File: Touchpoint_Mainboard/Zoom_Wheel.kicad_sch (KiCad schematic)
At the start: 7 parts

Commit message: Finished assigning footprints and 3d models for both boards
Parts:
- S1: footprint PEC12R-4220F-S0024:XDCR_PEC12R-4220F-S0024 -> Touchpoint:XDCR_PEC12R-4220F-S0024
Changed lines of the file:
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@@
 			)
 		)
-		(property "Footprint" "PEC12R-4220F-S0024:XDCR_PEC12R-4220F-S0024"
+		(property "Footprint" "Touchpoint:XDCR_PEC12R-4220F-S0024"
 			(at 68.58 38.1 0)
 			(effects

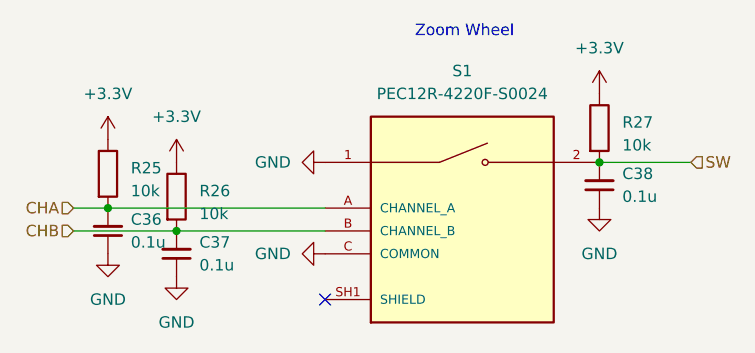
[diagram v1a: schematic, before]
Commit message: Added 3.3V to interface
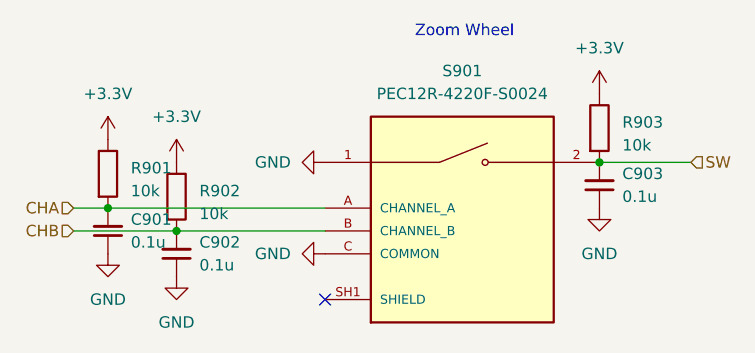
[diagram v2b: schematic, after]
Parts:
- renumbered C36 to C901, C37 to C902, C38 to C903, R25 to R901, R26 to R902, R27 to R903, S1 to S901
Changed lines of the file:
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@@
 		(dnp no)
 		(fields_autoplaced yes)
-		(property "Reference" "#PWR064"
+		(property "Reference" "#PWR0907"
 			(at 83.82 29.21 0)
 			(effects
@@
 			(project "Touchpoint_Mainboard"
 				(path "/f37b5f88-420a-4646-85df-8f9851d23e3c/eee90675-6c72-4499-ad3c-d412c9e5ddd7"
-					(reference "#PWR064")
+					(reference "#PWR0907")
 					(unit 1)
 				)
@@
 		(dnp no)
 		(fields_autoplaced yes)
-		(property "Reference" "#PWR069"
+		(property "Reference" "#PWR0906"
 			(at 46.99 43.18 0)
 			(effects
@@
 			(project "Touchpoint_Mainboard"
 				(path "/f37b5f88-420a-4646-85df-8f9851d23e3c/eee90675-6c72-4499-ad3c-d412c9e5ddd7"
-					(reference "#PWR069")
+					(reference "#PWR0906")
 					(unit 1)
 				)
@@
 		(dnp no)
 		(fields_autoplaced yes)
-		(property "Reference" "#PWR063"
+		(property "Reference" "#PWR0905"
 			(at 46.99 33.02 0)
 			(effects
@@
 			(project "Touchpoint_Mainboard"
 				(path "/f37b5f88-420a-4646-85df-8f9851d23e3c/eee90675-6c72-4499-ad3c-d412c9e5ddd7"
-					(reference "#PWR063")
+					(reference "#PWR0905")
 					(unit 1)
 				)
@@
 		(dnp no)
 		(fields_autoplaced yes)
-		(property "Reference" "#PWR072"
+		(property "Reference" "#PWR0902"
 			(at 29.21 49.53 0)
 			(effects
@@
 			(project "Touchpoint_Mainboard"
 				(path "/f37b5f88-420a-4646-85df-8f9851d23e3c/eee90675-6c72-4499-ad3c-d412c9e5ddd7"
-					(reference "#PWR072")
+					(reference "#PWR0902")
 					(unit 1)
 				)
@@
 		(dnp no)
 		(fields_autoplaced yes)
-		(property "Reference" "C37"
+		(property "Reference" "C902"
 			(at 39.37 41.9035 0)
 			(effects
@@
 			(project "Touchpoint_Mainboard"
 				(path "/f37b5f88-420a-4646-85df-8f9851d23e3c/eee90675-6c72-4499-ad3c-d412c9e5ddd7"
-					(reference "C37")
+					(reference "C902")
 					(unit 1)
 				)
@@
 		(dnp no)
 		(fields_autoplaced yes)
-		(property "Reference" "C36"
+		(property "Reference" "C901"
 			(at 31.75 39.3635 0)
 			(effects
@@
 			(project "Touchpoint_Mainboard"
 				(path "/f37b5f88-420a-4646-85df-8f9851d23e3c/eee90675-6c72-4499-ad3c-d412c9e5ddd7"
-					(reference "C36")
+					(reference "C901")
 					(unit 1)
 				)
@@
 		(dnp no)
 		(fields_autoplaced yes)
-		(property "Reference" "R25"
+		(property "Reference" "R901"
 			(at 31.75 33.655 0)
 			(effects
@@
 			(project "Touchpoint_Mainboard"
 				(path "/f37b5f88-420a-4646-85df-8f9851d23e3c/eee90675-6c72-4499-ad3c-d412c9e5ddd7"
-					(reference "R25")
+					(reference "R901")
 					(unit 1)
 				)
@@
 		(dnp no)
 		(fields_autoplaced yes)
-		(property "Reference" "#PWR071"
+		(property "Reference" "#PWR0903"
 			(at 36.83 36.83 0)
 			(effects
@@
 			(project "Touchpoint_Mainboard"
 				(path "/f37b5f88-420a-4646-85df-8f9851d23e3c/eee90675-6c72-4499-ad3c-d412c9e5ddd7"
-					(reference "#PWR071")
+					(reference "#PWR0903")
 					(unit 1)
 				)
@@
 		(dnp no)
 		(fields_autoplaced yes)
-		(property "Reference" "R26"
+		(property "Reference" "R902"
 			(at 39.37 36.195 0)
 			(effects
@@
 			(project "Touchpoint_Mainboard"
 				(path "/f37b5f88-420a-4646-85df-8f9851d23e3c/eee90675-6c72-4499-ad3c-d412c9e5ddd7"
-					(reference "R26")
+					(reference "R902")
 					(unit 1)
 				)
@@
 		(dnp no)
 		(fields_autoplaced yes)
-		(property "Reference" "C38"
+		(property "Reference" "C903"
 			(at 86.36 34.2835 0)
 			(effects
@@
 			(project "Touchpoint_Mainboard"
 				(path "/f37b5f88-420a-4646-85df-8f9851d23e3c/eee90675-6c72-4499-ad3c-d412c9e5ddd7"
-					(reference "C38")
+					(reference "C903")
 					(unit 1)
 				)
@@
 		(dnp no)
 		(fields_autoplaced yes)
-		(property "Reference" "R27"
+		(property "Reference" "R903"
 			(at 86.36 28.575 0)
 			(effects
@@
 			(project "Touchpoint_Mainboard"
 				(path "/f37b5f88-420a-4646-85df-8f9851d23e3c/eee90675-6c72-4499-ad3c-d412c9e5ddd7"
-					(reference "R27")
+					(reference "R903")
 					(unit 1)
 				)
@@
 		(dnp no)
 		(fields_autoplaced yes)
-		(property "Reference" "#PWR073"
+		(property "Reference" "#PWR0904"
 			(at 36.83 52.07 0)
 			(effects
@@
 			(project "Touchpoint_Mainboard"
 				(path "/f37b5f88-420a-4646-85df-8f9851d23e3c/eee90675-6c72-4499-ad3c-d412c9e5ddd7"
-					(reference "#PWR073")
+					(reference "#PWR0904")
 					(unit 1)
 				)
@@
 		(dnp no)
 		(fields_autoplaced yes)
-		(property "Reference" "#PWR070"
+		(property "Reference" "#PWR0901"
 			(at 29.21 34.29 0)
 			(effects
@@
 			(project "Touchpoint_Mainboard"
 				(path "/f37b5f88-420a-4646-85df-8f9851d23e3c/eee90675-6c72-4499-ad3c-d412c9e5ddd7"
-					(reference "#PWR070")
+					(reference "#PWR0901")
 					(unit 1)
 				)
@@
 		(dnp no)
 		(fields_autoplaced yes)
-		(property "Reference" "#PWR065"
+		(property "Reference" "#PWR0908"
 			(at 83.82 44.45 0)
 			(effects
@@
 			(project "Touchpoint_Mainboard"
 				(path "/f37b5f88-420a-4646-85df-8f9851d23e3c/eee90675-6c72-4499-ad3c-d412c9e5ddd7"
-					(reference "#PWR065")
+					(reference "#PWR0908")
 					(unit 1)
 				)
@@
 		(dnp no)
 		(fields_autoplaced yes)
-		(property "Reference" "S1"
+		(property "Reference" "S901"
 			(at 68.58 22.86 0)
 			(effects
@@
 			(project "Touchpoint_Mainboard"
 				(path "/f37b5f88-420a-4646-85df-8f9851d23e3c/eee90675-6c72-4499-ad3c-d412c9e5ddd7"
-					(reference "S1")
-					(unit 1)
-				)
+					(reference "S901")
+					(unit 1)
+				)
